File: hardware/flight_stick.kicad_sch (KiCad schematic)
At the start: 22 parts, among them J10 USB_C_Receptacle_USB2.0, J2 Conn_02x05_Top_Bottom, J9 Conn_ST_STDC14, SW1 KMR223G LFG, U2 AT24CS01-MAHM, U4 STM32F103CBU6, U5 USBLC6-2SC6, Y1 8M

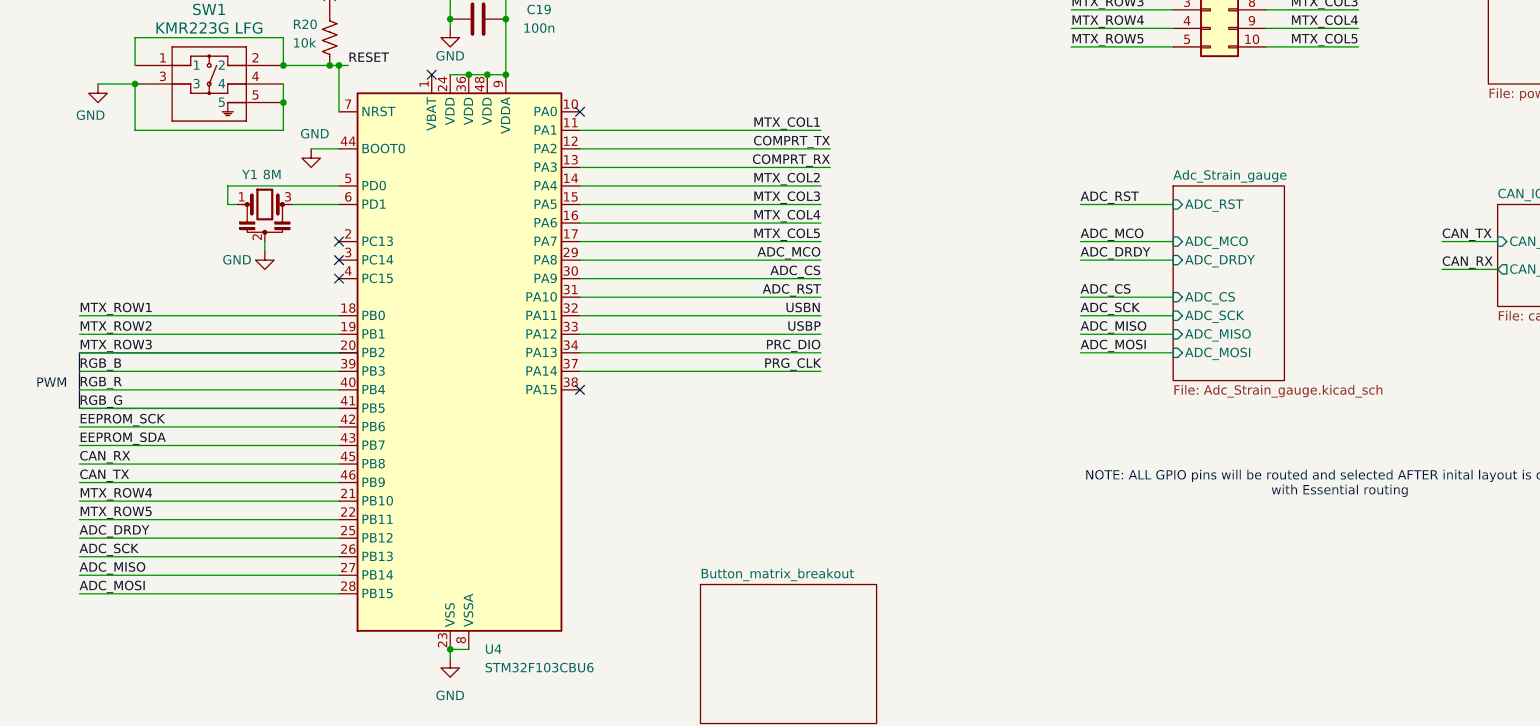
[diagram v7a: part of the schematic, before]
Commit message: modified mcu pin alloc and pre-routing placement
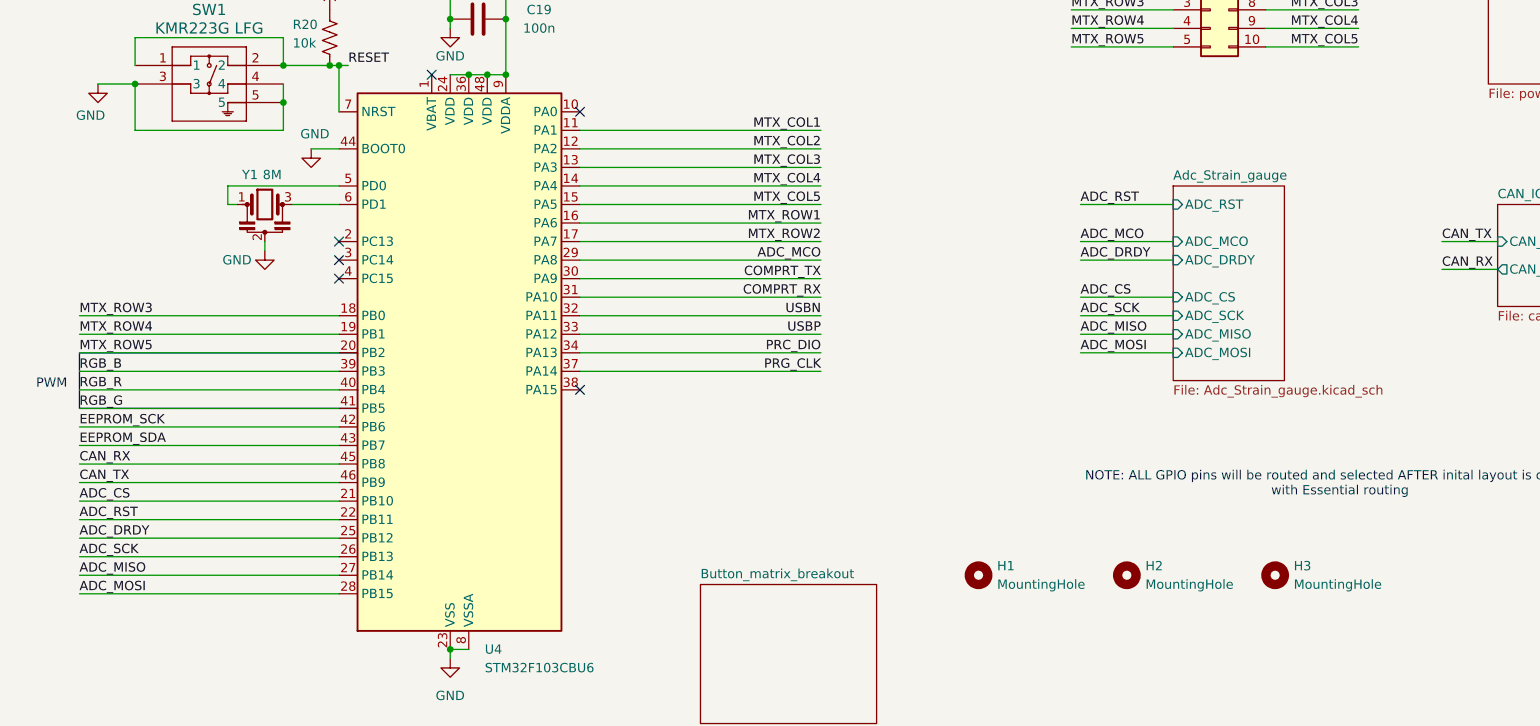
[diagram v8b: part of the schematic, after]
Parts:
- added H1, H2, H3: MountingHole, MountingHole:MountingHole_3.2mm_M3, symbol Mechanical:MountingHole
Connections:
- net ADC_CS: now also U4.21 (PB10); no longer U4.30 (PA9)
- net ADC_RST: now also U4.22 (PB11); no longer U4.31 (PA10)
- net COMPRT_RX: now also U4.31 (PA10); no longer U4.13 (PA3)
- net COMPRT_TX: now also U4.30 (PA9); no longer U4.12 (PA2)
- net MTX_COL2: now also U4.12 (PA2); no longer U4.14 (PA4)
- net MTX_COL3: now also U4.13 (PA3); no longer U4.15 (PA5)
- net MTX_COL4: now also U4.14 (PA4); no longer U4.16 (PA6)
- net MTX_COL5: now also U4.15 (PA5); no longer U4.17 (PA7)
- net MTX_ROW1: now also U4.16 (PA6); no longer U4.18 (PB0)
- net MTX_ROW2: now also U4.17 (PA7); no longer U4.19 (PB1)
- net MTX_ROW3: now also U4.18 (PB0); no longer U4.20 (PB2)
- net MTX_ROW4: now also U4.19 (PB1); no longer U4.21 (PB10)
- net MTX_ROW5: now also U4.20 (PB2); no longer U4.22 (PB11)
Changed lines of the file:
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@@
 	(wire
 		(pts
-			(xy 107.95 111.76) (xy 142.24 111.76)
+			(xy 107.95 111.76) (xy 140.97 111.76)
 		)
 		(stroke
@@
 	(wire
 		(pts
-			(xy 107.95 109.22) (xy 142.24 109.22)
+			(xy 107.95 109.22) (xy 140.97 109.22)
 		)
 		(stroke
@@
 		)
 	)
-	(label "MTX_COL4"
-		(at 140.97 119.38 180)
+	(label "COMPRT_TX"
+		(at 140.97 127 180)
 		(effects
 			(font
@@
 		)
 	)
-	(label "MTX_ROW4"
-		(at 39.37 157.48 0)
-		(effects
-			(font
-				(size 1.27 1.27)
-			)
-			(justify left bottom)
-		)
-	)
 	(label "MTX_COL3"
-		(at 140.97 116.84 180)
+		(at 140.97 111.76 180)
 		(effects
 			(font
@@
 		)
 	)
-	(label "MTX_ROW3"
-		(at 39.37 137.16 0)
+	(label "MTX_COL5"
+		(at 140.97 116.84 180)
 		(effects
 			(font
 				(size 1.27 1.27)
 			)
-			(justify left bottom)
+			(justify right bottom)
 		)
 	)
-	(label "MTX_COL3"
-		(at 214.63 90.17 180)
+	(label "MTX_ROW2"
+		(at 140.97 121.92 180)
 		(effects
 			(font
@@
 		)
 	)
-	(label "MTX_ROW5"
-		(at 39.37 160.02 0)
+	(label "MTX_COL3"
+		(at 214.63 90.17 180)
 		(effects
 			(font
 				(size 1.27 1.27)
 			)
-			(justify left bottom)
+			(justify right bottom)
 		)
 	)
@@
 		)
 	)
+	(label "MTX_ROW1"
+		(at 140.97 119.38 180)
+		(effects
+			(font
+				(size 1.27 1.27)
+			)
+			(justify right bottom)
+		)
+	)
 	(label "D+"
 		(at 222.25 46.99 0)
@@
 		)
 	)
-	(label "MTX_ROW2"
+	(label "MTX_ROW4"
 		(at 39.37 134.62 0)
 		(effects
@@
 		)
 	)
-	(label "RGB_G"
-		(at 39.37 144.78 0)
+	(label "ADC_CS"
+		(at 39.37 157.48 0)
 		(effects
 			(font
@@
 		)
 	)
-	(label "CAN_TX"
-		(at 39.37 154.94 0)
+	(label "RGB_G"
+		(at 39.37 144.78 0)
 		(effects
 			(font
@@
 		)
 	)
-	(label "ADC_RST"
-		(at 140.97 129.54 180)
+	(label "CAN_TX"
+		(at 39.37 154.94 0)
 		(effects
 			(font
 				(size 1.27 1.27)
 			)
-			(justify right bottom)
+			(justify left bottom)
 		)
 	)
@@
 		)
 	)
+	(label "ADC_RST"
+		(at 39.37 160.02 0)
+		(effects
+			(font
+				(size 1.27 1.27)
+			)
+			(justify left bottom)
+		)
+	)
 	(label "ADC_SCK"
 		(at 39.37 165.1 0)
@@
 		)
 	)
-	(label "MTX_ROW1"
-		(at 39.37 132.08 0)
-		(effects
-			(font
-				(size 1.27 1.27)
-			)
-			(justify left bottom)
-		)
-	)
 	(label "USBN"
 		(at 140.97 132.08 180)
@@
 		)
 	)
-	(label "COMPRT_RX"
-		(at 179.07 53.34 180)
+	(label "MTX_ROW5"
+		(at 39.37 137.16 0)
+		(effects
+			(font
+				(size 1.27 1.27)
+			)
+			(justify left bottom)
+		)
+	)
+	(label "MTX_COL2"
+		(at 140.97 109.22 180)
 		(effects
 			(font
@@
 		)
 	)
-	(label "MTX_COL5"
-		(at 140.97 121.92 180)
+	(label "MTX_COL4"
+		(at 140.97 114.3 180)
+		(effects
+			(font
+				(size 1.27 1.27)
+			)
+			(justify right bottom)
+		)
+	)
+	(label "COMPRT_RX"
+		(at 179.07 53.34 180)
 		(effects
 			(font
@@
 		)
 	)
-	(label "COMPRT_TX"
-		(at 142.24 109.22 180)
+	(label "EEPROM_SCK"
+		(at 39.37 147.32 0)
 		(effects
 			(font
 				(size 1.27 1.27)
 			)
-			(justify right bottom)
+			(justify left bottom)
 		)
 	)
-	(label "EEPROM_SCK"
-		(at 39.37 147.32 0)
+	(label "COMPRT_RX"
+		(at 140.97 129.54 180)
 		(effects
 			(font
 				(size 1.27 1.27)
 			)
-			(justify left bottom)
+			(justify right bottom)
 		)
 	)
@@
 		)
 	)
-	(label "RGB_R"
-		(at 39.37 142.24 0)
+	(label "MTX_ROW3"
+		(at 39.37 132.08 0)
 		(effects
 			(font
@@
 		)
 	)
-	(label "PRC_DIO"
-		(at 176.53 38.1 180)
+	(label "RGB_R"
+		(at 39.37 142.24 0)
 		(effects
 			(font
 				(size 1.27 1.27)
 			)
-			(justify right bottom)
+			(justify left bottom)
 		)
 	)
-	(label "ADC_CS"
-		(at 140.97 127 180)
+	(label "PRC_DIO"
+		(at 176.53 38.1 180)
 		(effects
 			(font
@@
 		)
 	)
-	(label "COMPRT_RX"
-		(at 142.24 111.76 180)
-		(effects
-			(font
-				(size 1.27 1.27)
-			)
-			(justify right bottom)
-		)
-	)
-	(label "MTX_COL2"
-		(at 140.97 114.3 180)
-		(effects
-			(font
-				(size 1.27 1.27)
-			)
-			(justify right bottom)
-		)
-	)
 	(label "CAN_RX"
 		(at 226.06 125.73 0)
@@
 	)
 	(symbol
+		(lib_id "Mechanical:MountingHole")
+		(at 162.56 167.64 0)
+		(unit 1)
+		(exclude_from_sim no)
+		(in_bom no)
+		(on_board yes)
+		(dnp no)
+		(fields_autoplaced yes)
+		(property "Reference" "H1"
+			(at 165.1 166.3699 0)
+			(effects
+				(font
+					(size 1.27 1.27)
+				)
+				(justify left)
+			)
+		)
+		(property "Value" "MountingHole"
+			(at 165.1 168.9099 0)
+			(effects
+				(font
+					(size 1.27 1.27)
+				)
+				(justify left)
+			)
+		)
+		(property "Footprint" "MountingHole:MountingHole_3.2mm_M3"
+			(at 162.56 167.64 0)
+			(effects
+				(font
+					(size 1.27 1.27)
+				)
+				(hide yes)
+			)
+		)
+		(property "Datasheet" "~"
+			(at 162.56 167.64 0)
+			(effects
+				(font
+					(size 1.27 1.27)
+				)
+				(hide yes)
+			)
+		)
+		(property "Description" "Mounting Hole without connection"
+			(at 162.56 167.64 0)
+			(effects
+				(font
+					(size 1.27 1.27)
+				)
+				(hide yes)
+			)
+		)
+		(instances
+			(project ""
+				(path "/594f9b09-cd7b-4dfb-a8eb-b099e26ad96c"
+					(reference "H1")
+					(unit 1)
+				)
+			)
+		)
+	)
+	(symbol
 		(lib_id "power:+3.3V")
 		(at 153.67 24.13 0)
@@
 	)
 	(symbol
+		(lib_id "Mechanical:MountingHole")
+		(at 182.88 167.64 0)
+		(unit 1)
+		(exclude_from_sim no)
+		(in_bom no)
+		(on_board yes)
+		(dnp no)
+		(fields_autoplaced yes)
+		(property "Reference" "H2"
+			(at 185.42 166.3699 0)
+			(effects
+				(font
+					(size 1.27 1.27)
+				)
+				(justify left)
+			)
+		)
+		(property "Value" "MountingHole"
+			(at 185.42 168.9099 0)
+			(effects
+				(font
+					(size 1.27 1.27)
+				)
+				(justify left)
+			)
+		)
+		(property "Footprint" "MountingHole:MountingHole_3.2mm_M3"
+			(at 182.88 167.64 0)
+			(effects
+				(font
+					(size 1.27 1.27)
+				)
+				(hide yes)
+			)
+		)
+		(property "Datasheet" "~"
+			(at 182.88 167.64 0)
+			(effects
+				(font
+					(size 1.27 1.27)
+				)
+				(hide yes)
+			)
+		)
+		(property "Description" "Mounting Hole without connection"
+			(at 182.88 167.64 0)
+			(effects
+				(font
+					(size 1.27 1.27)
+				)
+				(hide yes)
+			)
+		)
+		(instances
+			(project "flight_stick"
+				(path "/594f9b09-cd7b-4dfb-a8eb-b099e26ad96c"
+					(reference "H2")
+					(unit 1)
+				)
+			)
+		)
+	)
+	(symbol
 		(lib_id "Device:R_US")
 		(at 73.66 93.98 0)
@@
 					(unit 1)
 				)
+			)
+		)
+	)
+	(symbol
+		(lib_id "Mechanical:MountingHole")
+		(at 203.2 167.64 0)
+		(unit 1)
+		(exclude_from_sim no)
+		(in_bom no)
+		(on_board yes)
+		(dnp no)
+		(fields_autoplaced yes)
+		(property "Reference" "H3"
+			(at 205.74 166.3699 0)
+			(effects
+				(font
+					(size 1.27 1.27)
+				)
+				(justify left)
+			)
+		)
+		(property "Value" "MountingHole"
+			(at 205.74 168.9099 0)
+			(effects
+				(font
+					(size 1.27 1.27)
+				)
+				(justify left)
+			)
+		)
+		(property "Footprint" "MountingHole:MountingHole_3.2mm_M3"
+			(at 203.2 167.64 0)
+			(effects
+				(font
+					(size 1.27 1.27)
+				)
+				(hide yes)
+			)
+		)
+		(property "Datasheet" "~"
+			(at 203.2 167.64 0)
+			(effects
+				(font
+					(size 1.27 1.27)
+				)
+				(hide yes)
+			)
+		)
+		(property "Description" "Mounting Hole without connection"
+			(at 203.2 167.64 0)
+			(effects
+				(font
+					(size 1.27 1.27)
+				)
+				(hide yes)
+			)
+		)
+		(instances
+			(project "flight_stick"
+				(path "/594f9b09-cd7b-4dfb-a8eb-b099e26ad96c"
+					(reference "H3")
+					(unit 1)
+				)
